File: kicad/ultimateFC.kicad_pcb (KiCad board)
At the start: 8 copper layers, 30.4 x 25.2 mm, 193 parts, among them J1 USB_B_Micro, J2 10132797-011100LF, J3 10132797-011100LF, J4 10132797-011100LF, J5 10132797-011100LF, J6 10132797-011100LF, Q1 DMP2066LSN-7, U1 EFM8BB21F16G-C-QFN20R, U10 NCP81253MNTBG, U11 SiZ200DT, U12 NCP81253MNTBG, U13 SiZ200DT, U14 TPS62824ADMQ, U15 SiZ200DT, U16 NCP81253MNTBG, U17 NCP81253MNTBG, U18 NCP81253MNTBG, U19 NCP81253MNTBG, U2 EFM8BB21F16G-C-QFN20R, U20 SiZ200DT, U21 SiZ200DT, U22 SiZ200DT, U23 SiZ200DT, U24 EFM8BB21F16G-C-QFN20R, U25 NCP81253MNTBG, U26 SiZ200DT, U27 NCP81253MNTBG, U28 NCP81253MNTBG, U29 SiZ200DT, U3 NCP81253MNTBG, U30 SiZ200DT, U31 INA186, U32 LMR33630CQRNX, U33 STM32F745VGHx, U34 AB7456, U35 ZOE-M8Q_ZOE-M8Q, U36 ICM-20602, U37 S25FL064L, U39 BMP280, U4 SiZ200DT, U6 EFM8BB21F16G-C-QFN20R, U7 NCP81253MNTBG, U8 SiZ200DT, U9 NCP81253MNTBG, X1 Molex_734120110, Y1 CSTNE8M00G550000R0, Y2 ECS-270-8-47Q-CES-TR

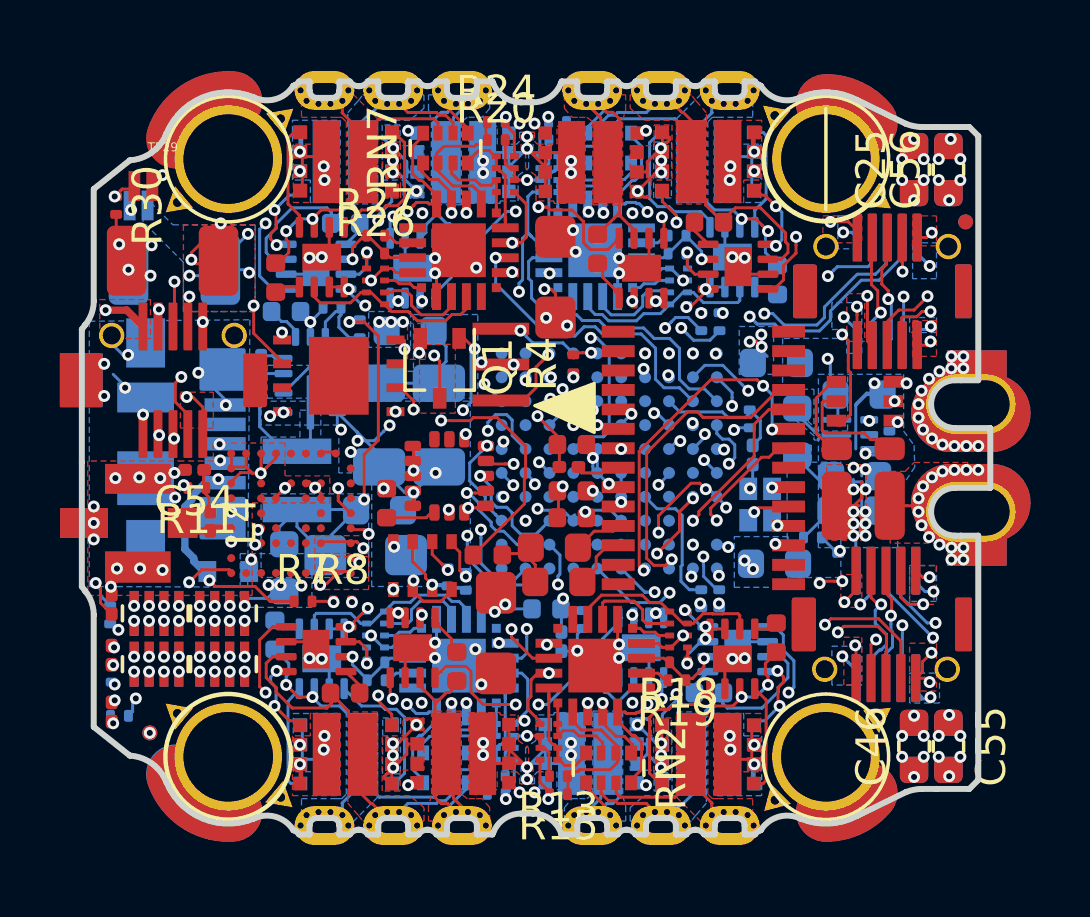
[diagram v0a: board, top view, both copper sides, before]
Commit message: swap ESC gate role names, add schematic pdf
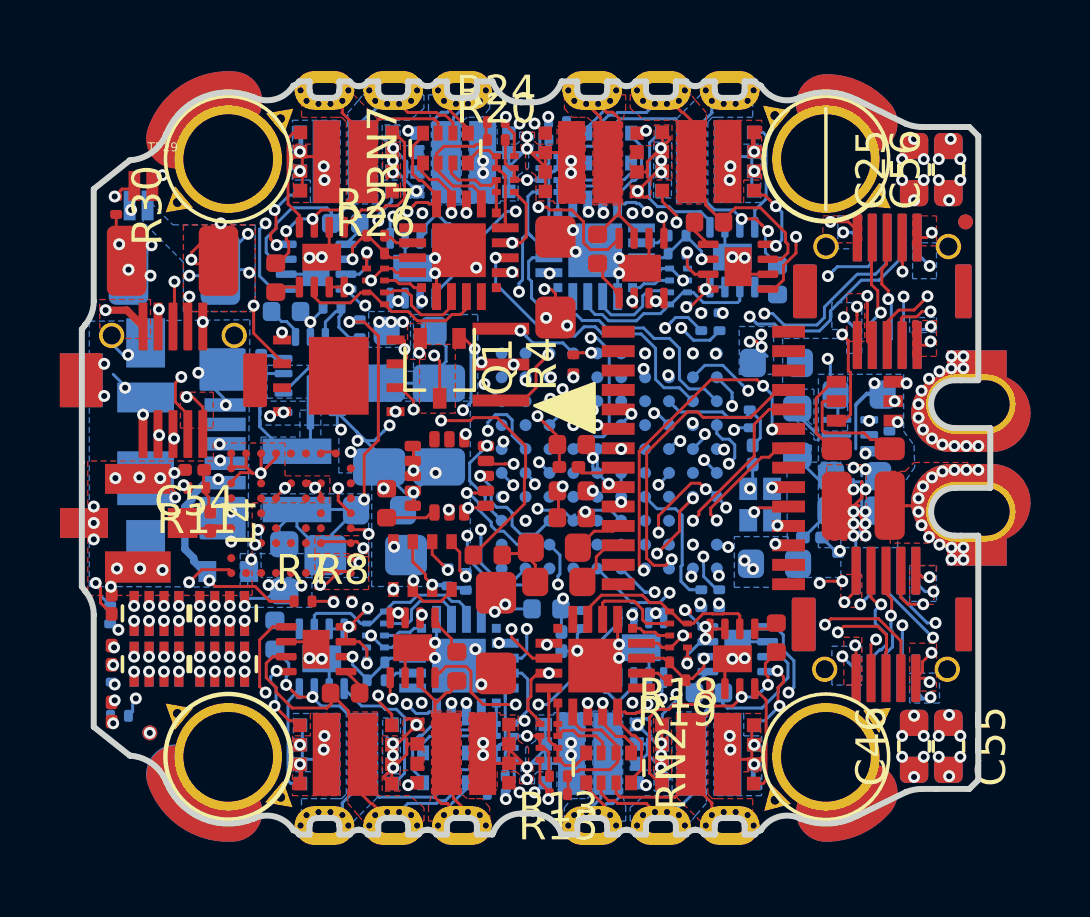
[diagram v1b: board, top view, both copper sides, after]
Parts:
- removed the REF** at (197.1, 64.1) (x2)
- added REF**: Fiducial_0.5mm_Dia_1mm_Outer, Fiducial:Fiducial_0.5mm_Dia_1mm_Outer, F.Cu at (197.1, 64.1)
- added REF**: Fiducial_0.5mm_Dia_1mm_Outer, Fiducial:Fiducial_0.5mm_Dia_1mm_Outer, B.Cu at (197.1, 64.1)
- C53: footprint ultimateFC:R_0201_0603Metric_mod -> Capacitor_SMD:C_0201_0603Metric
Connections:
- R16 pad 2: Cp_ESC_1 -> Cc_ESC_1
- R17 pad 1: Cp_ESC_1 -> Cc_ESC_1
- R17 pad 2: Cc_ESC_1 -> Cp_ESC_1
- R18 pad 2: Cp_ESC_3 -> Cc_ESC_3
- R19 pad 1: Cp_ESC_3 -> Cc_ESC_3
- R19 pad 2: Cc_ESC_3 -> Cp_ESC_3
- R26 pad 2: Cp_ESC_2 -> Cc_ESC_2
- R27 pad 1: Cp_ESC_2 -> Cc_ESC_2
- R27 pad 2: Cc_ESC_2 -> Cp_ESC_2
- R28 pad 2: Cp_ESC_4 -> Cc_ESC_4
- R29 pad 1: Cp_ESC_4 -> Cc_ESC_4
- R29 pad 2: Cc_ESC_4 -> Cp_ESC_4
- RN13 pad 2: Bp_ESC_2 -> Bc_ESC_2
- RN13 pad 3: Ap_ESC_2 -> Ac_ESC_2
- RN13 pad 5: Ap_ESC_2 -> Ac_ESC_2
- RN13 pad 6: Ac_ESC_2 -> Ap_ESC_2
- RN13 pad 7: Bc_ESC_2 -> Bp_ESC_2
- RN13 pad 8: Bp_ESC_2 -> Bc_ESC_2
- RN14 pad 2: Bp_ESC_1 -> Bc_ESC_1
- RN14 pad 3: Ap_ESC_1 -> Ac_ESC_1
- RN14 pad 5: Ap_ESC_1 -> Ac_ESC_1
- RN14 pad 6: Ac_ESC_1 -> Ap_ESC_1
- RN14 pad 7: Bc_ESC_1 -> Bp_ESC_1
- RN14 pad 8: Bp_ESC_1 -> Bc_ESC_1
- RN15 pad 2: Bp_ESC_3 -> Bc_ESC_3
- RN15 pad 3: Ap_ESC_3 -> Ac_ESC_3
- RN15 pad 5: Ap_ESC_3 -> Ac_ESC_3
- RN15 pad 6: Ac_ESC_3 -> Ap_ESC_3
- RN15 pad 7: Bc_ESC_3 -> Bp_ESC_3
- RN15 pad 8: Bp_ESC_3 -> Bc_ESC_3
- RN20 pad 2: Bp_ESC_4 -> Bc_ESC_4
- RN20 pad 3: Ap_ESC_4 -> Ac_ESC_4
- RN20 pad 5: Ap_ESC_4 -> Ac_ESC_4
- RN20 pad 6: Ac_ESC_4 -> Ap_ESC_4
- RN20 pad 7: Bc_ESC_4 -> Bp_ESC_4
- RN20 pad 8: Bp_ESC_4 -> Bc_ESC_4
- U1 pad 10: Bp_ESC_1 -> Bc_ESC_1
- U1 pad 11: Bc_ESC_1 -> Bp_ESC_1
- U1 pad 13: Ac_ESC_1 -> Ap_ESC_1
- U1 pad 14: Ap_ESC_1 -> Ac_ESC_1
- U1 pad 8: Cc_ESC_1 -> Cp_ESC_1
- U1 pad 9: Cp_ESC_1 -> Cc_ESC_1
- U10 pad 2: Bp_ESC_1 -> Bc_ESC_1
- U12 pad 2: Bp_ESC_3 -> Bc_ESC_3
- U16 pad 2: Cp_ESC_1 -> Cc_ESC_1
- U17 pad 2: Cp_ESC_3 -> Cc_ESC_3
- U18 pad 2: Ap_ESC_1 -> Ac_ESC_1
- U19 pad 2: Ap_ESC_3 -> Ac_ESC_3
- U2 pad 10: Bp_ESC_2 -> Bc_ESC_2
- U2 pad 11: Bc_ESC_2 -> Bp_ESC_2
- U2 pad 13: Ac_ESC_2 -> Ap_ESC_2
- U2 pad 14: Ap_ESC_2 -> Ac_ESC_2
- U2 pad 8: Cc_ESC_2 -> Cp_ESC_2
- U2 pad 9: Cp_ESC_2 -> Cc_ESC_2
- U24 pad 10: Bp_ESC_4 -> Bc_ESC_4
- U24 pad 11: Bc_ESC_4 -> Bp_ESC_4
- U24 pad 13: Ac_ESC_4 -> Ap_ESC_4
- U24 pad 14: Ap_ESC_4 -> Ac_ESC_4
- U24 pad 8: Cc_ESC_4 -> Cp_ESC_4
- U24 pad 9: Cp_ESC_4 -> Cc_ESC_4
- U25 pad 2: Bp_ESC_4 -> Bc_ESC_4
- U27 pad 2: Cp_ESC_4 -> Cc_ESC_4
- U28 pad 2: Ap_ESC_4 -> Ac_ESC_4
- U3 pad 2: Ap_ESC_2 -> Ac_ESC_2
- U6 pad 10: Bp_ESC_3 -> Bc_ESC_3
- U6 pad 11: Bc_ESC_3 -> Bp_ESC_3
- U6 pad 13: Ac_ESC_3 -> Ap_ESC_3
- U6 pad 14: Ap_ESC_3 -> Ac_ESC_3
- U6 pad 8: Cc_ESC_3 -> Cp_ESC_3
- U6 pad 9: Cp_ESC_3 -> Cc_ESC_3
- U7 pad 2: Bp_ESC_2 -> Bc_ESC_2
- U9 pad 2: Cp_ESC_2 -> Cc_ESC_2
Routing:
- net Ap_ESC_4: track 7.03 -> 3.29 mm
- net Ac_ESC_4: track 3.29 -> 7.03 mm
- net Ap_ESC_1: track 7.03 -> 3.34 mm
- net Ac_ESC_1: track 3.34 -> 7.03 mm
- net Ap_ESC_2: track 7.01 -> 3.32 mm
- net Ac_ESC_2: track 3.32 -> 7.01 mm
- net Ap_ESC_3: track 7.03 -> 3.42 mm
- net Ac_ESC_3: track 3.42 -> 7.03 mm
- net Bp_ESC_2: track 4.45 -> 1.34 mm, vias 2 -> 0
- net Bc_ESC_2: track 1.34 -> 4.45 mm, vias 0 -> 2
- net Bp_ESC_4: track 4.44 -> 1.34 mm, vias 2 -> 0
- net Bc_ESC_4: track 1.34 -> 4.44 mm, vias 0 -> 2
- net Bp_ESC_3: track 4.44 -> 1.34 mm, vias 2 -> 0
- net Bp_ESC_1: track 4.44 -> 1.34 mm, vias 2 -> 0
- net Bc_ESC_3: track 1.34 -> 4.44 mm, vias 0 -> 2
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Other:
- board text removed: "VREGs nach rechts schieben USB auf bottom setzen"

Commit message: exported gerbers and p+p files, started whoop mount adapter
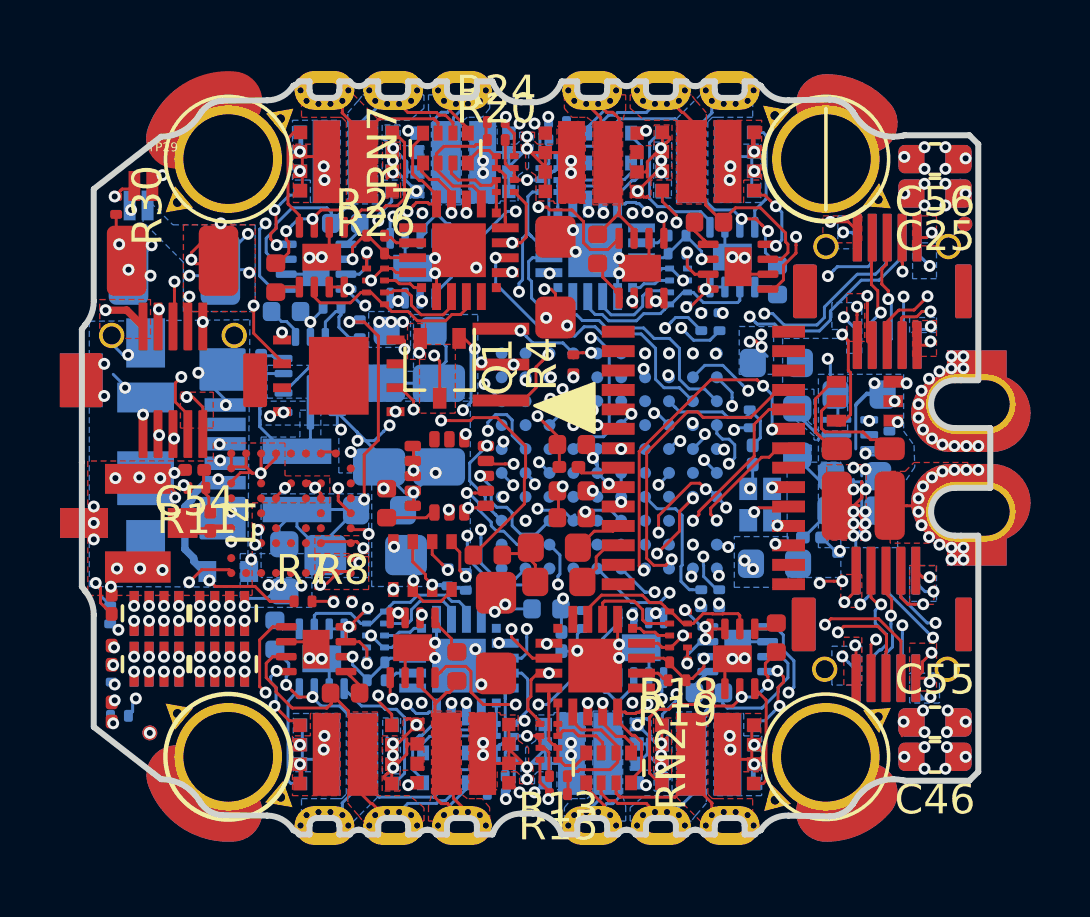
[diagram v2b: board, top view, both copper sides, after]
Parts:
- removed the REF** at (197.1, 64.1) (x2)
- added REF**: Fiducial_0.5mm_Dia_1mm_Outer, Fiducial:Fiducial_0.5mm_Dia_1mm_Outer, F.Cu at (197.1, 64.2)
- added REF**: Fiducial_0.5mm_Dia_1mm_Outer, Fiducial:Fiducial_0.5mm_Dia_1mm_Outer, B.Cu at (197.1, 64.2)
- moved C23 1.06 mm to (196.2, 63.1), turned to 180 degrees
- moved C25 1.06 mm to (196.2, 63.1), turned to 180 degrees
- moved C24 0.92 mm to (196.2, 80.8), turned to 180 degrees
- moved C55 0.92 mm to (196.2, 80.8), turned to 0 degrees
- moved C22 0.78 mm to (196.2, 82.0), turned to 0 degrees
- moved C46 0.78 mm to (196.2, 82.0), turned to 180 degrees
- moved C45 0.57 mm to (196.2, 62.0), turned to 180 degrees
- moved C56 0.57 mm to (196.2, 62.0), turned to 180 degrees
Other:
- outline, holes or cut-outs redrawn
- board text added: "If you want to (commercially) manufacture this, we strongly recommend to contact us before ( yolofc@weber-ee.de )."
- board text added: "Please use the correct layer stackup, via in pad and sideplating options."
- board text added: "Sideplating"
- board text added: "When using this commercially, please be fair and mention our names ( crteensy / chris_fly ) on some prominet place"

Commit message: added diode on 5V DCDC input
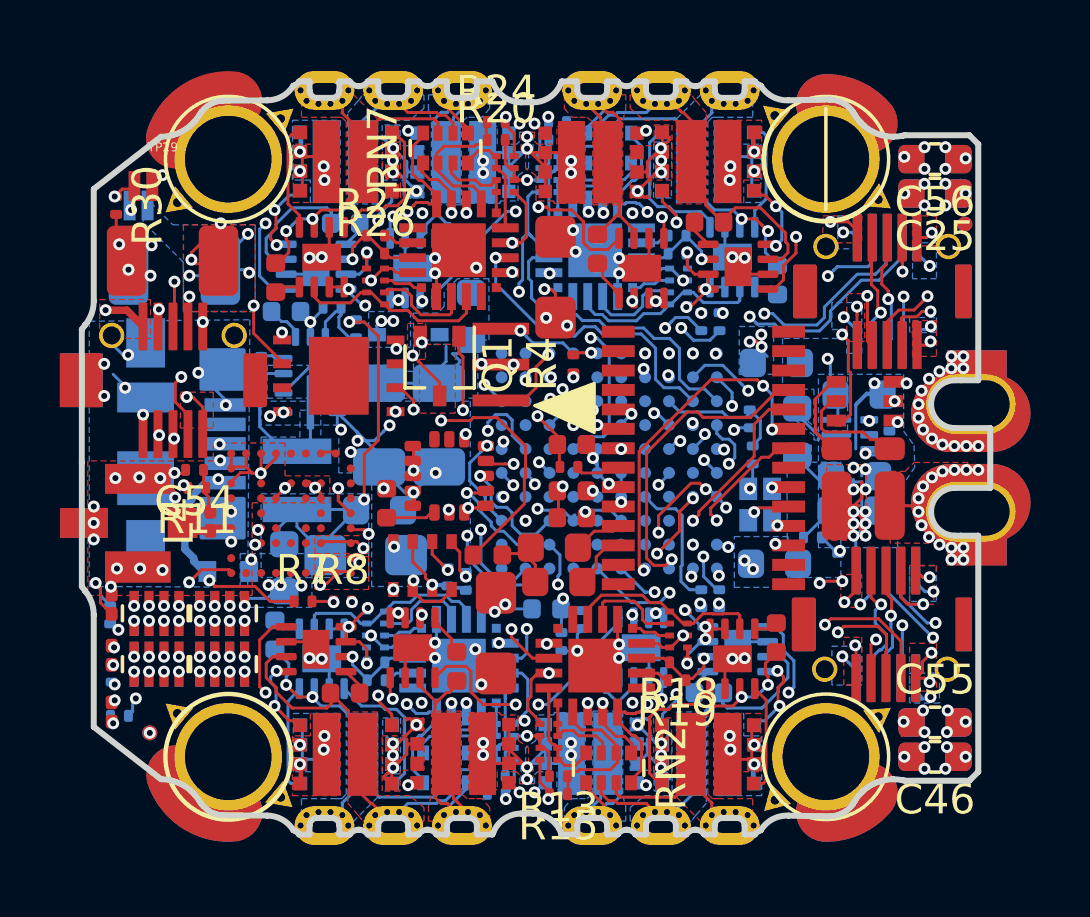
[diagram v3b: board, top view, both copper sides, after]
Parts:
- removed the REF** at (197.1, 64.2) (x2)
- added D101: PMEG3020EJ,115, Diode_SMD:D_SOD-323, B.Cu at (178.5, 67.9)
- added REF**: Fiducial_0.5mm_Dia_1mm_Outer, Fiducial:Fiducial_0.5mm_Dia_1mm_Outer, F.Cu at (197.1, 64.2)
- added REF**: Fiducial_0.5mm_Dia_1mm_Outer, Fiducial:Fiducial_0.5mm_Dia_1mm_Outer, B.Cu at (197.1, 64.2)
- C28, C33, C38, C47, C53, C54: footprint Capacitor_SMD:C_0201_0603Metric -> ultimateFC:C_0201_0603Metric_mod
- moved FB5 2.10 mm to (180.6, 67.3), turned to 270 degrees
- moved R1 0.12 mm to (176.8, 67.7)
- moved Q1 0.08 mm to (179.6, 68.9)
- turned L4 to 90 degrees
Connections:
- FB5 pad 1: Net-(C35-Pad1) -> Net-(D101-Pad1)
- FB5 pad 2: +BATT -> Net-(C35-Pad1)
- L4 pad 1: Net-(C54-Pad1) -> Net-(L4-Pad1)
- L4 pad 2: Net-(L4-Pad2) -> Net-(C54-Pad1)
- U35 pad P$A4: Net-(L4-Pad2) -> Net-(L4-Pad1)
- X1 pad 1: Net-(L4-Pad2) -> Net-(L4-Pad1)
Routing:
- net Net-(L4-Pad2): track 1.77 -> 0.00 mm
- net Net-(L4-Pad1): track 0.00 -> 1.77 mm
- net Net-(C35-Pad1): track 9.22 -> 10.8 mm
- net USB_VBUS: track 26.0 -> 25.7 mm, vias 4 -> 3
- net +BATT: track 64.5 -> 64.6 mm, vias 63 -> 62
- added copper zone on B.Cu, net Net-(D101-Pad1)

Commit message: changed some minor pcb things
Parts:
- removed the REF** at (197.1, 64.2) (x2)
- added REF**: Fiducial_0.5mm_Dia_1mm_Outer, Fiducial:Fiducial_0.5mm_Dia_1mm_Outer, F.Cu at (197.1, 64.2)
- added REF**: Fiducial_0.5mm_Dia_1mm_Outer, Fiducial:Fiducial_0.5mm_Dia_1mm_Outer, B.Cu at (197.1, 64.2)
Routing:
- net Net-(C35-Pad1): track 10.8 -> 9.97 mm
- net +5V: track 36.0 -> 36.7 mm, vias 45 -> 46
- net Net-(J6-Pad10): track 18.7 -> 19.5 mm, vias 4 -> 5
